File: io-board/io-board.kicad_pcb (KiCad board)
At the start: 2 copper layers, 104.1 x 67.3 mm, 12 parts, among them J1 Expansion, J2 Expansion, J3 Conn_01x12, J4 Conn_01x12, J5 Conn_01x06, U1 W65C22NxP, U2 W65C51NxP, U3 74HC138, X1 1.8432MHz

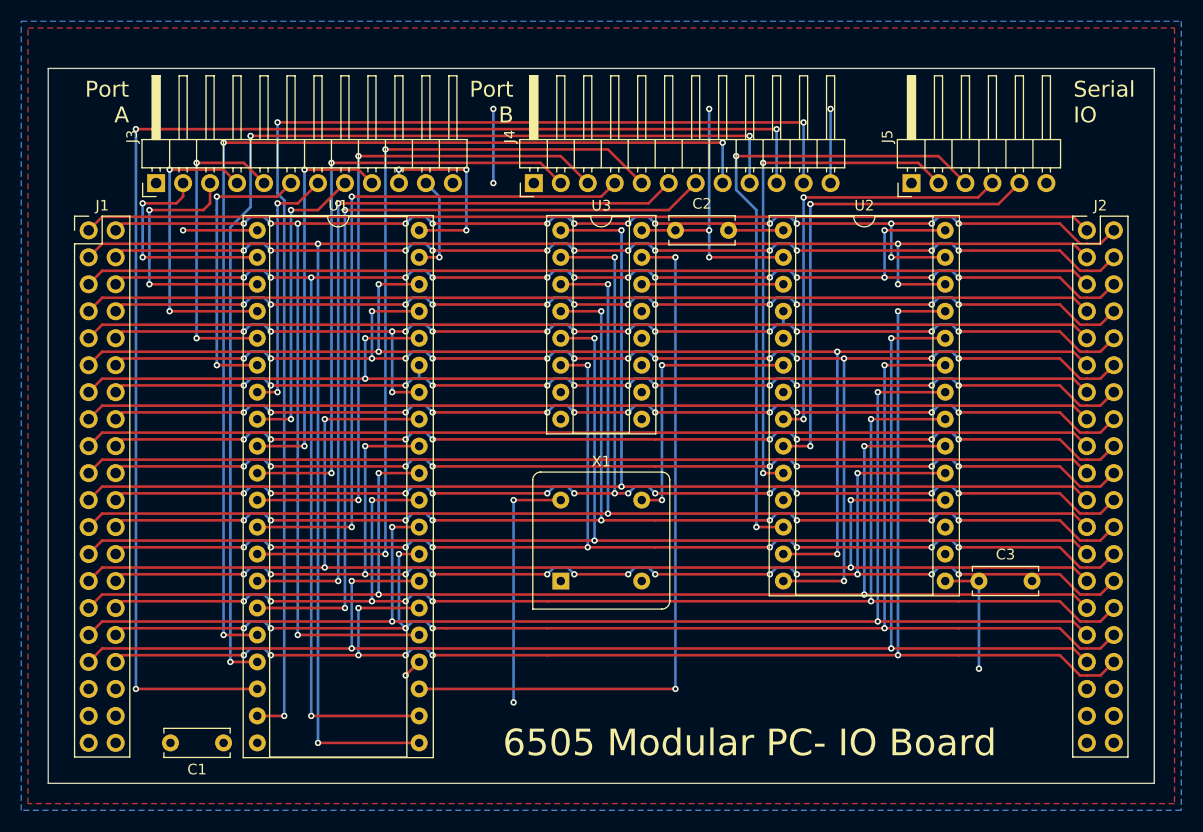
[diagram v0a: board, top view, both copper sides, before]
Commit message: remove vga board, finish other boards
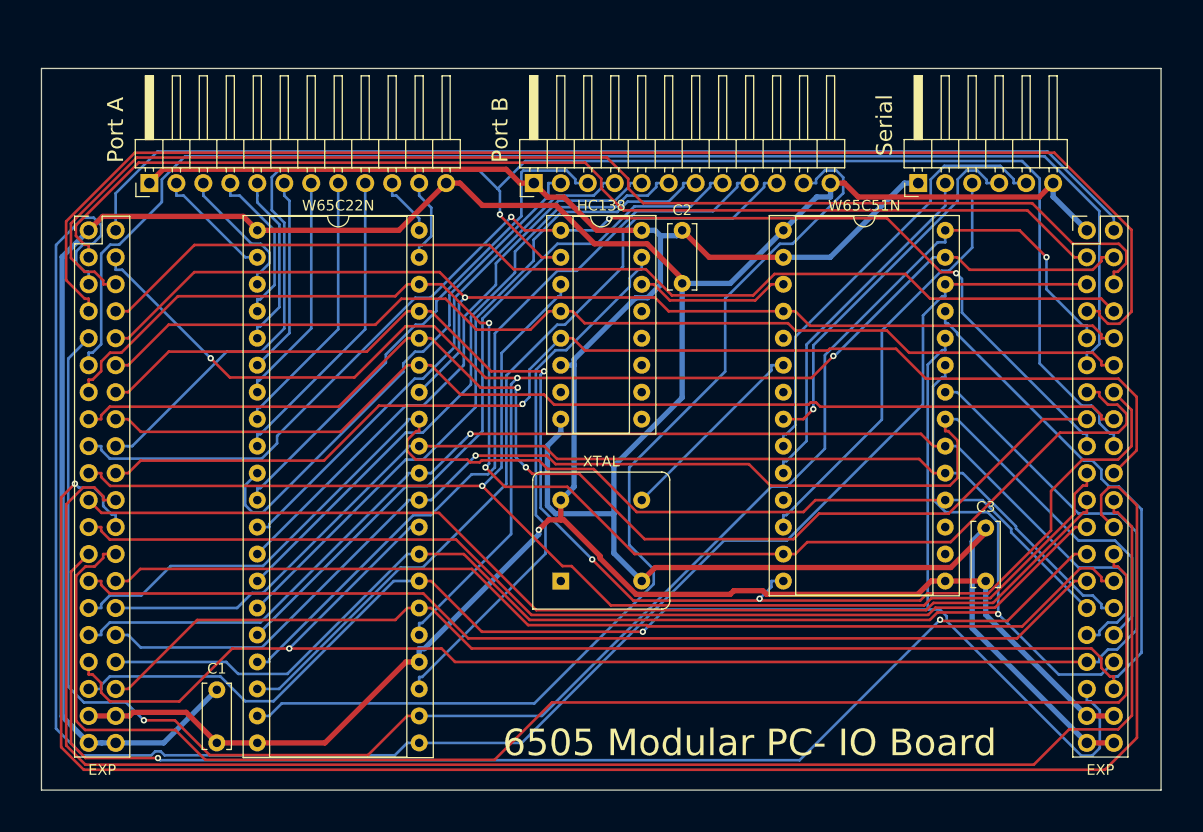
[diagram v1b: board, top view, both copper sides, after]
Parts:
- moved C3 0.64 mm to (130.2, 99.1), turned to 90 degrees
- moved C1 0.64 mm to (57.8, 114.3), turned to 90 degrees
- moved J5 0.64 mm to (123.8, 61.6)
- moved J3 0.63 mm to (51.4, 61.6)
- moved C2 0.63 mm to (101.6, 66.0), turned to 270 degrees
- renumbered J2 to EXP, J1 to EXP, U3 to HC138, U1 to W65C22N, U2 to W65C51N, X1 to XTAL
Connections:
- EXP pad 1: PHI1 -> GND (x2)
- EXP pad 11: A0 -> RDY (x2)
- EXP pad 12: A1 -> !P_SELECT (x2)
- EXP pad 13: A2 -> A0 (x2)
- EXP pad 14: A3 -> A1 (x2)
- EXP pad 15: A4 -> A2 (x2)
- EXP pad 16: A5 -> A3 (x2)
- EXP pad 17: A6 -> A4 (x2)
- EXP pad 18: A7 -> A5 (x2)
- EXP pad 19: A8 -> A6 (x2)
- EXP pad 2: PHI2 -> CLK (x2)
- EXP pad 20: A9 -> A7 (x2)
- EXP pad 21: A10 -> A8 (x2)
- EXP pad 22: A11 -> A9 (x2)
- EXP pad 23: A12 -> A10 (x2)
- EXP pad 24: A13 -> A11 (x2)
- EXP pad 25: A14 -> A12 (x2)
- EXP pad 26: A15 -> A13 (x2)
- EXP pad 27: D0 -> A14 (x2)
- EXP pad 28: D1 -> A15 (x2)
- EXP pad 29: D2 -> D0 (x2)
- EXP pad 3: !IRQ -> PHI1 (x2)
- EXP pad 30: D3 -> D1 (x2)
- EXP pad 31: D4 -> D2 (x2)
- EXP pad 32: D5 -> D3 (x2)
- EXP pad 33: D6 -> D4 (x2)
- EXP pad 34: D7 -> D5 (x2)
- EXP pad 35: +5V -> D6 (x2)
- EXP pad 36: +5V -> D7 (x2)
- EXP pad 37: GND -> +5V (x2)
- EXP pad 38: GND -> +5V (x2)
- EXP pad 4: !NMI -> PHI2 (x2)
- EXP pad 5: RDY -> !IRQ (x2)
- EXP pad 6: R!W -> !NMI (x2)
- EXP pad 7: !WRITE -> !READ (x2)
- EXP pad 8: !READ -> !WRITE (x2)
- EXP pad 9: CLK -> R!W (x2)
- HC138 pad 1: A10 -> A4
- HC138 pad 2: A11 -> A5
- HC138 pad 3: A12 -> A6
- HC138 pad 4: A13 -> !P_SELECT
- HC138 pad 5: A14 -> A7
- HC138 pad 6: A15 -> +5V
- J4 pad 12: +5V -> GND
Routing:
- net GND: track 12.1 -> 283.4 mm, vias 1 -> 0
- net +5V: track 78.0 -> 230.7 mm, vias 10 -> 1
- net !P_SELECT: track 0.00 -> 100.8 mm
- net A9: track 97.7 -> 152.9 mm, vias 8 -> 0
- net CB1: track 129.5 -> 76.8 mm, vias 3 -> 0
- net A5: track 98.7 -> 149.1 mm, vias 12 -> 1
- net A11: track 126.0 -> 165.3 mm, vias 14 -> 1
- net A6: track 95.0 -> 128.5 mm, vias 0 -> 1
- net RDY: track 95.0 -> 127.6 mm
- net PB6: track 100.3 -> 67.9 mm, vias 3 -> 0
- net PB7: track 104.3 -> 72.8 mm, vias 3 -> 0
- net !READ: track 98.7 -> 128.6 mm, vias 12 -> 0
- net D1: track 133.6 -> 107.1 mm, vias 16 -> 0
- net A10: track 124.9 -> 101.0 mm, vias 2 -> 0
- net A4: track 95.0 -> 116.9 mm, vias 0 -> 3
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- removed copper zone on F.Cu, net +5V
- removed copper zone on B.Cu, net GND
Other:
- board size 104.1 x 67.3 mm -> 105.4 x 67.9 mm
- net class Wide added: clearance 0.2, trace_width 0.5, via_dia 0.6, via_drill 0.3
- board text added: "JLCJLCJLCJLC"
- board text added: "Serial"
- board text removed: "Serial IO"

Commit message: Fix IO board routing errors
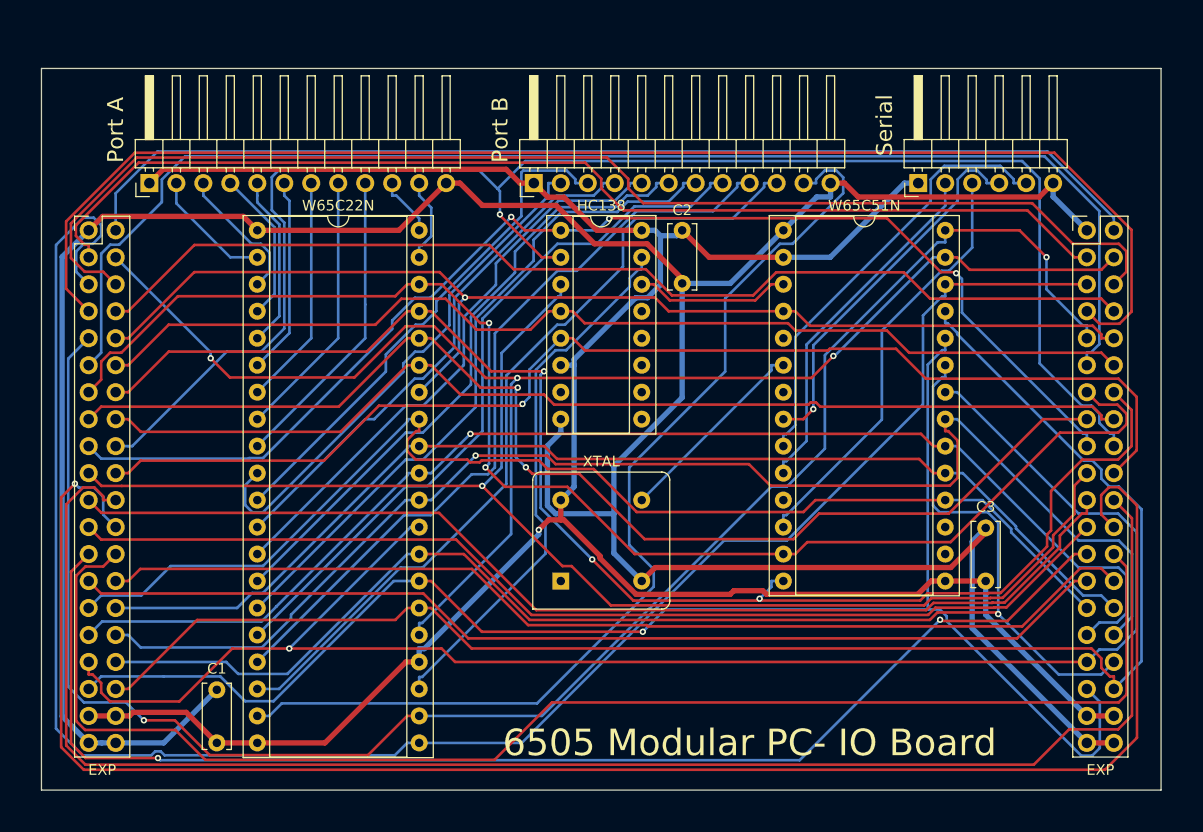
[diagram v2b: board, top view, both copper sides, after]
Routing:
- net A8: track 103.3 -> 104.0 mm
- net PA2: track 15.1 -> 14.5 mm
- net A1: track 135.4 -> 136.1 mm
- net PHI2: track 137.5 -> 136.9 mm

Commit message: Redesign CPU and IO boards
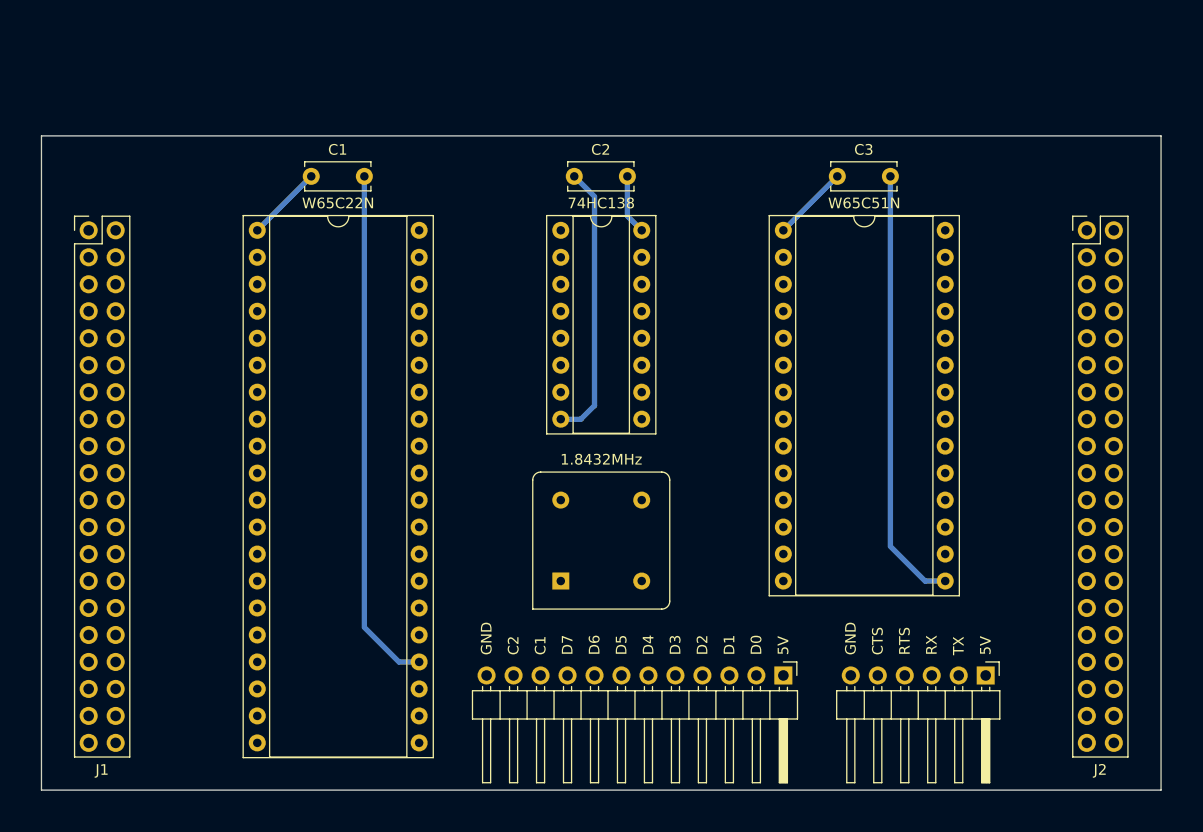
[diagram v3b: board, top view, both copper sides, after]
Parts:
- removed HC138: 74HC138, Package_DIP:DIP-16_W7.62mm_Socket
- removed J4: Conn_01x12, Connector_PinHeader_2.54mm:PinHeader_1x12_P2.54mm_Horizontal
- removed XTAL: 1.8432MHz, Oscillator:Oscillator_DIP-8
- added U2: 74HC138, Package_DIP:DIP-16_W7.62mm_Socket, F.Cu at (90.2, 66.0)
- added X1: 1.8432MHz, Oscillator:Oscillator_DIP-8, F.Cu at (90.2, 99.1)
- U1: renamed from W65C22N; value W65C22NxP -> W65C22N
- U3: renamed from W65C51N; value W65C51NxP -> W65C51N
- moved J3 75.6 mm to (111.1, 108.0), turned to 270 degrees
- moved C1 54.1 mm to (66.7, 61.0), turned to 0 degrees
- moved J5 46.8 mm to (130.2, 108.0), turned to 270 degrees
- moved C3 40.6 mm to (116.2, 61.0), turned to 0 degrees
- moved C2 11.4 mm to (91.4, 61.0), turned to 0 degrees
- renumbered EXP to J1, EXP to J2
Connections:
- C1 pad 1: +5V -> GND
- C1 pad 2: GND -> +5V
- C2 pad 1: +5V -> GND
- C2 pad 2: GND -> +5V
- C3 pad 1: +5V -> GND
- C3 pad 2: GND -> +5V
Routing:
- net GND: track 283.4 -> 40.4 mm
- net !IRQ: track 181.0 -> 0.00 mm
- net R!W: track 165.1 -> 0.00 mm, vias 2 -> 0
- net A11: track 165.0 -> 0.00 mm, vias 1 -> 0
- net D4: track 154.9 -> 0.00 mm, vias 1 -> 0
- net A9: track 152.7 -> 0.00 mm
- net A5: track 149.1 -> 0.00 mm, vias 1 -> 0
- net D7: track 146.9 -> 0.00 mm
- net D6: track 142.9 -> 0.00 mm, vias 1 -> 0
- net PHI2: track 136.9 -> 0.00 mm, vias 3 -> 0
- net A1: track 136.1 -> 0.00 mm, vias 3 -> 0
- net A13: track 134.9 -> 0.00 mm
- net +5V: track 230.7 -> 96.0 mm, vias 1 -> 0
- net D5: track 134.2 -> 0.00 mm, vias 1 -> 0
- net A0: track 132.5 -> 0.00 mm, vias 2 -> 0
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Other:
- board size 105.4 x 67.9 mm -> 105.4 x 61.6 mm
- board text added: "5V"
- board text added: "C1"
- board text added: "C2"
- board text added: "CTS"
- board text added: "D0"
- board text added: "D1"
- board text added: "D2"
- board text added: "D3"
- board text added: "D4"
- board text added: "D5"
- board text added: "D6"
- board text added: "D7"
- board text added: "GND"
- board text added: "RTS"
- board text added: "RX"
- board text added: "TX"
- board text removed: "6505 Modular PC- IO Board"
- board text removed: "Port A"
- board text removed: "Port B"
- board text removed: "Serial"

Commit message: Finish designing and routing new CPU and IO boards
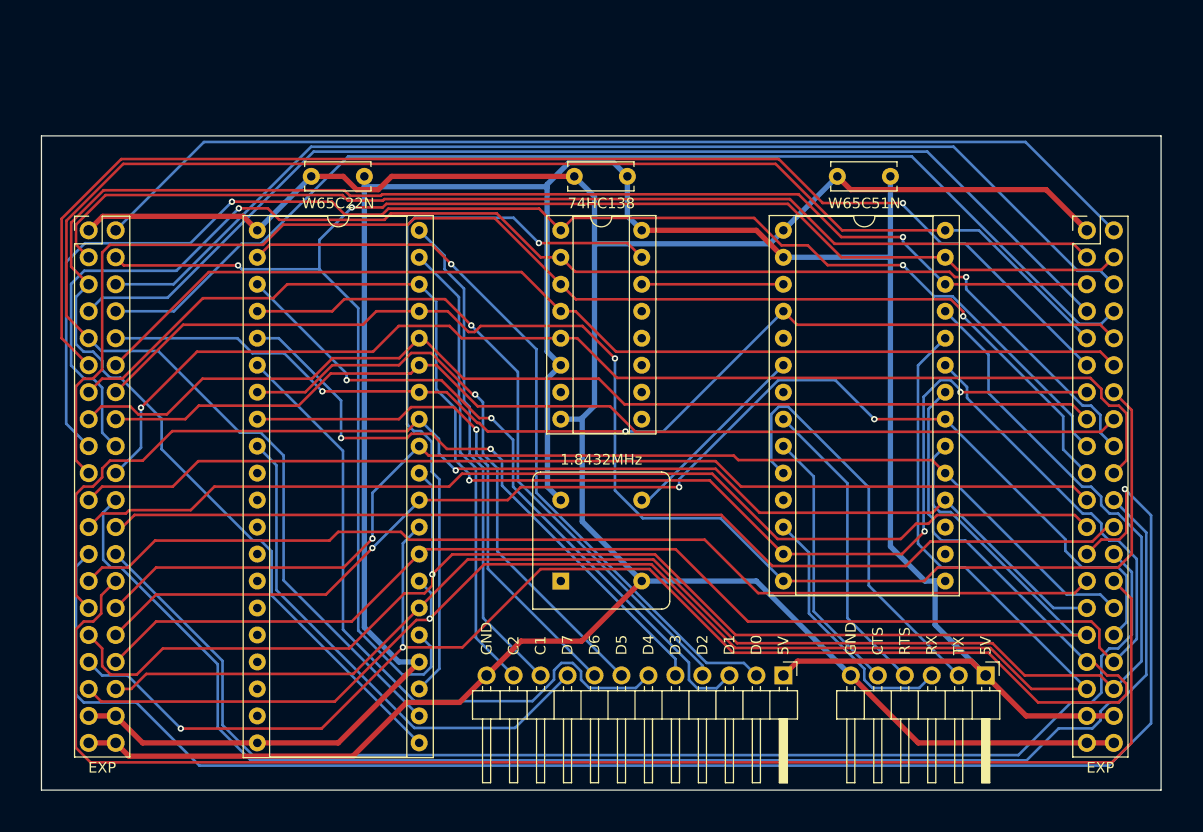
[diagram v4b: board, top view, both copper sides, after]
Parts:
- J1, J2: value Expansion -> EXP
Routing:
- net GND: track 40.4 -> 255.0 mm
- net R!W: track 0.00 -> 169.8 mm
- net !IRQ: track 0.00 -> 166.0 mm, vias 0 -> 1
- net D4: track 0.00 -> 163.1 mm, vias 0 -> 2
- net +5V: track 96.0 -> 257.9 mm
- net A12: track 0.00 -> 151.2 mm, vias 0 -> 1
- net D6: track 0.00 -> 150.7 mm, vias 0 -> 1
- net PHI2: track 0.00 -> 149.6 mm, vias 0 -> 2
- net D7: track 0.00 -> 149.3 mm
- net D5: track 0.00 -> 141.0 mm
- net D2: track 0.00 -> 140.5 mm, vias 0 -> 1
- net A9: track 0.00 -> 137.2 mm
- net A15: track 0.00 -> 134.4 mm
- net A1: track 0.00 -> 134.1 mm, vias 0 -> 1
- net A0: track 0.00 -> 131.7 mm, vias 0 -> 3
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
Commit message: remove old peripheral boards, begn new vga design
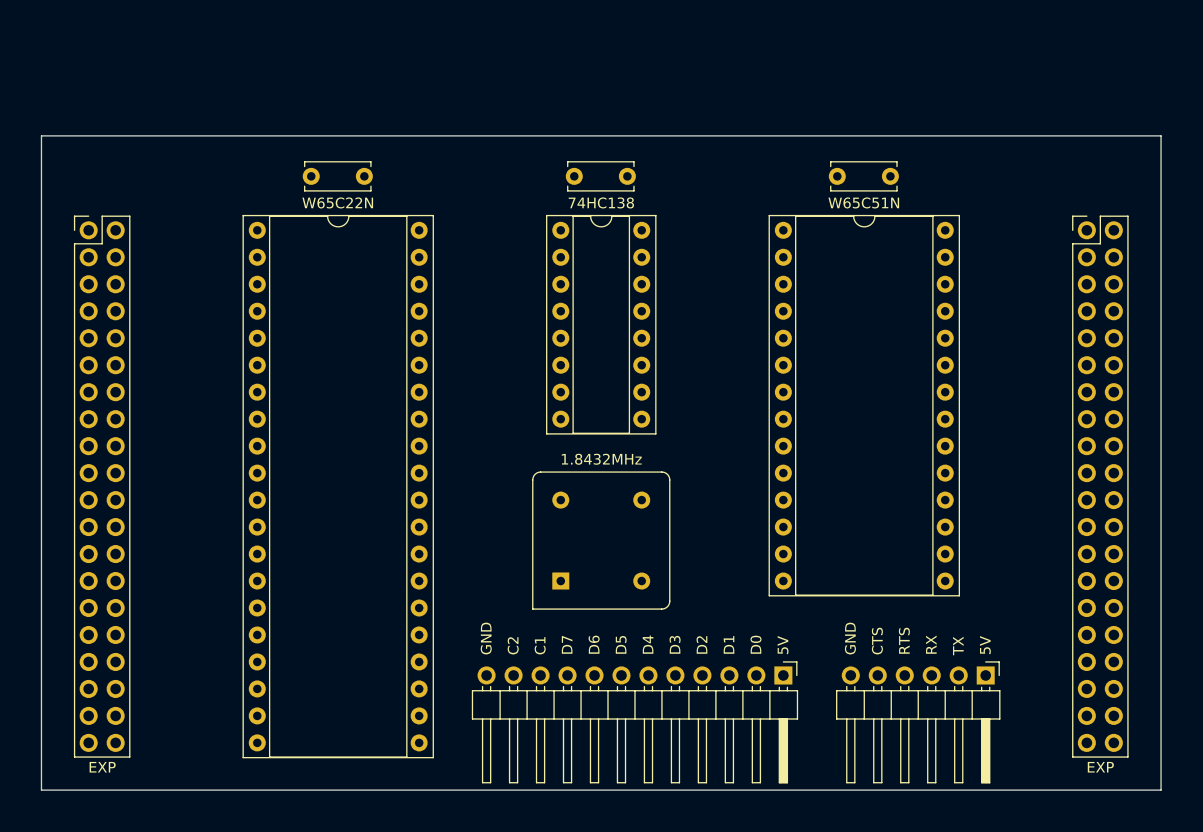
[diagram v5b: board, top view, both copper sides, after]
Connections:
- J1 pad 1: GND -> PHI1
- J1 pad 10: !RESET -> CLK
- J1 pad 11: RDY -> GND
- J1 pad 12: !P_SELECT -> GND
- J1 pad 2: CLK -> PHI2
- J1 pad 3: PHI1 -> !IRQ
- J1 pad 4: PHI2 -> !NMI
- J1 pad 5: !IRQ -> !READ
- J1 pad 6: !NMI -> !WRITE
- J1 pad 7: !READ -> R!W
- J1 pad 8: !WRITE -> !RESET
- J1 pad 9: R!W -> RDY
- J2 pad 1: GND -> PHI1
- J2 pad 10: !RESET -> CLK
- J2 pad 11: RDY -> GND
- J2 pad 12: !P_SELECT -> GND
- J2 pad 2: CLK -> PHI2
- J2 pad 3: PHI1 -> !IRQ
- J2 pad 4: PHI2 -> !NMI
- J2 pad 5: !IRQ -> !READ
- J2 pad 6: !NMI -> !WRITE
- J2 pad 7: !READ -> R!W
- J2 pad 8: !WRITE -> !RESET
- J2 pad 9: R!W -> RDY
- U2 pad 4: !P_SELECT -> A7
- U2 pad 5: A7 -> A14
- U2 pad 6: +5V -> A15
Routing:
- net +5V: track 257.9 -> 0.00 mm
- net GND: track 255.0 -> 0.00 mm
- net R!W: track 169.8 -> 0.00 mm
- net !IRQ: track 166.0 -> 0.00 mm, vias 1 -> 0
- net D4: track 163.1 -> 0.00 mm, vias 2 -> 0
- net A12: track 151.2 -> 0.00 mm, vias 1 -> 0
- net D6: track 150.7 -> 0.00 mm, vias 1 -> 0
- net PHI2: track 149.6 -> 0.00 mm, vias 2 -> 0
- net D7: track 149.3 -> 0.00 mm
- net D5: track 141.0 -> 0.00 mm
- net D2: track 140.5 -> 0.00 mm, vias 1 -> 0
- net A9: track 137.2 -> 0.00 mm
- net A15: track 134.4 -> 0.00 mm
- net A1: track 134.1 -> 0.00 mm, vias 1 -> 0
- net A0: track 131.7 -> 0.00 mm, vias 3 -> 0
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
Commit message: reroute main board and IO board again
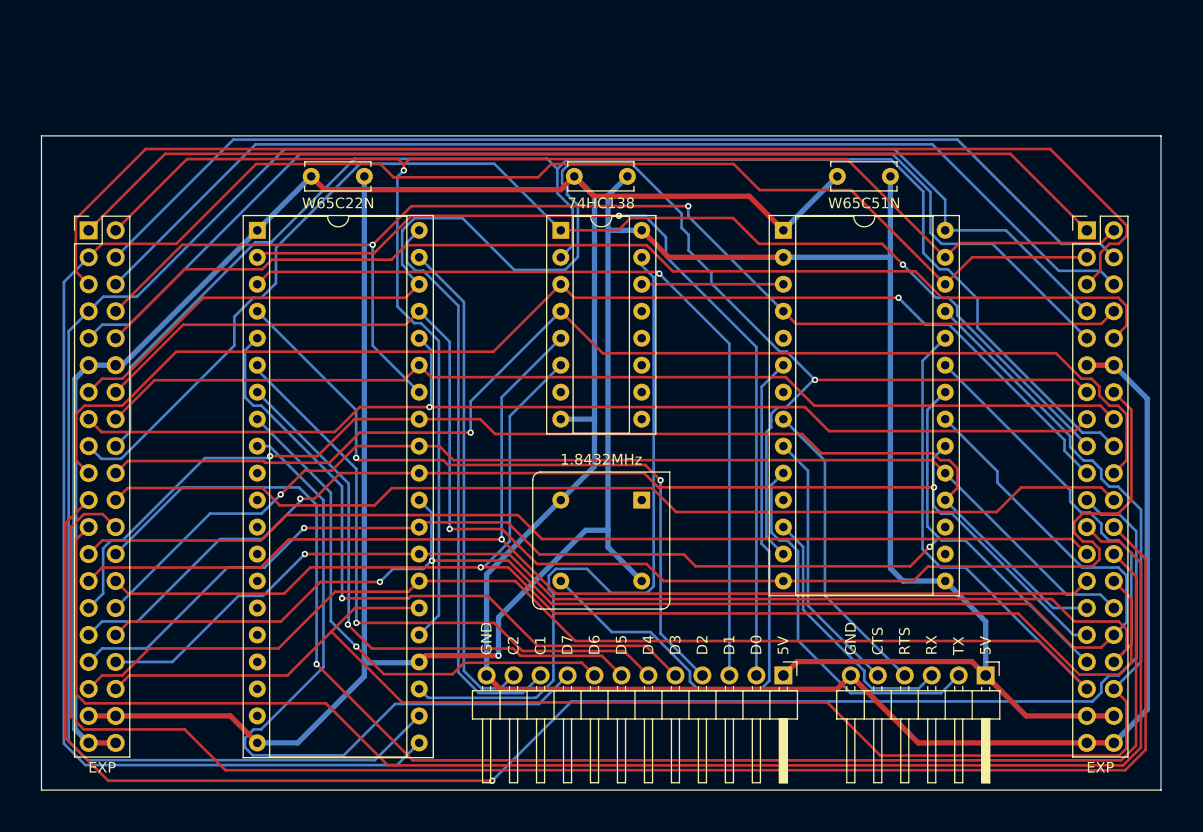
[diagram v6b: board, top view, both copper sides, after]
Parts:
- moved X1 10.8 mm to (97.8, 91.4), turned to 180 degrees
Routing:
- net GND: track 0.00 -> 280.9 mm
- net +5V: track 0.00 -> 261.5 mm, vias 0 -> 1
- net !IRQ: track 0.00 -> 186.3 mm
- net R!W: track 0.00 -> 185.0 mm
- net D7: track 0.00 -> 163.0 mm
- net A0: track 0.00 -> 149.5 mm, vias 0 -> 1
- net PHI2: track 0.00 -> 149.4 mm, vias 0 -> 1
- net A11: track 0.00 -> 149.3 mm
- net A8: track 0.00 -> 148.9 mm, vias 0 -> 1
- net D6: track 0.00 -> 144.1 mm
- net A10: track 0.00 -> 143.9 mm
- net D5: track 0.00 -> 142.8 mm, vias 0 -> 1
- net A1: track 0.00 -> 139.6 mm, vias 0 -> 1
- net A13: track 0.00 -> 137.6 mm, vias 0 -> 1
- net D3: track 0.00 -> 136.8 mm, vias 0 -> 2
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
